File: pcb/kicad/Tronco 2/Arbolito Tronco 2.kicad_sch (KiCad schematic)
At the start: 18 parts, among them U1 WS2812B, U10 WS2812B, U11 WS2812B, U12 WS2812B, U2 WS2812B, U3 WS2812B, U4 WS2812B, U5 WS2812B, U6 WS2812B, U7 WS2812B, U8 WS2812B, U9 WS2812B

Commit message: Do some cleaning and add .gitignore
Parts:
- removed C3, C4: 0.1uF, Capacitor_SMD:C_0805_2012Metric, symbol Device:C
- removed U1, U11, U12, U2, U5, U6, U7, U8: WS2812B, LED_SMD:LED_WS2812B_PLCC4_5.0x5.0mm_P3.2mm, symbol WB2182:WS2812B
- added J1, J2, J3, J4, J5, J6: Conn_01x01, Library:Output, symbol Connector_Generic:Conn_01x01
- U1: renamed from U3; footprint LED_SMD:LED_WS2812B_PLCC4_5.0x5.0mm_P3.2mm -> Library:LED_WS2812B_PLCC4_5.0x5.0mm_P3.2mm
- U2: renamed from U4; footprint LED_SMD:LED_WS2812B_PLCC4_5.0x5.0mm_P3.2mm -> Library:LED_WS2812B_PLCC4_5.0x5.0mm_P3.2mm
- U3: renamed from U9; footprint LED_SMD:LED_WS2812B_PLCC4_5.0x5.0mm_P3.2mm -> Library:LED_WS2812B_PLCC4_5.0x5.0mm_P3.2mm
- U4: renamed from U10; footprint LED_SMD:LED_WS2812B_PLCC4_5.0x5.0mm_P3.2mm -> Library:LED_WS2812B_PLCC4_5.0x5.0mm_P3.2mm
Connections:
- net +5V: now also J3.1 (Pin_1), J4.1 (Pin_1)
- net DIN: now also U1.4 (DIN), J1.1 (Pin_1), J2.1 (Pin_1)
- net GND: now also J5.1 (Pin_1), J6.1 (Pin_1)
- net at U2.2 (DOUT): now also U3.4 (DIN)

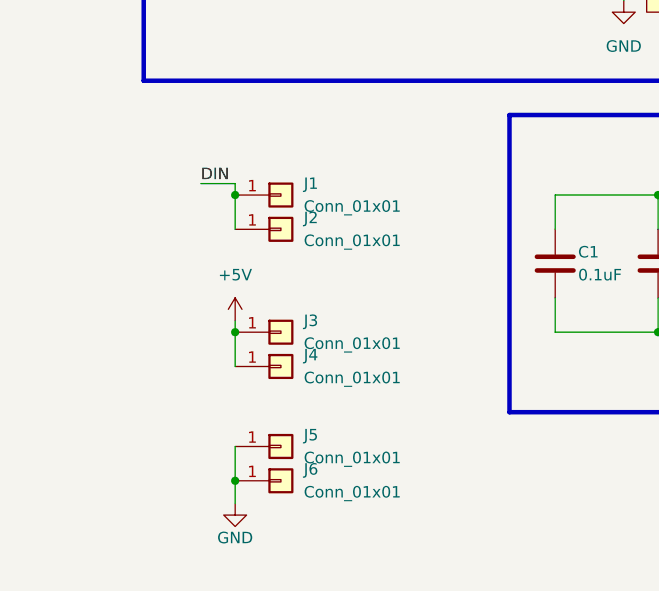
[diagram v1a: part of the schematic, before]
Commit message: DRC Errors fixeds
The WS218B double footprint was remade in order to avoid DRC errors :3
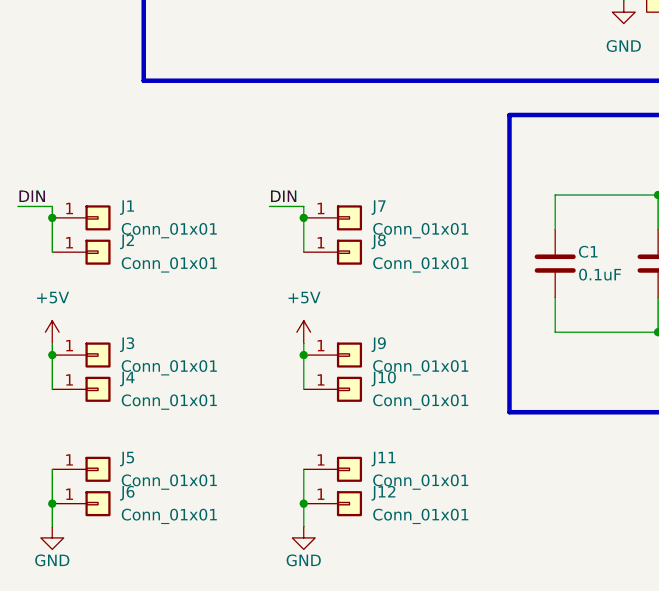
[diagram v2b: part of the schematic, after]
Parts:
- added J10, J11, J12, J7, J8, J9: Conn_01x01, Library:Output, symbol Connector_Generic:Conn_01x01
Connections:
- net +5V: now also J10.1 (Pin_1), J9.1 (Pin_1)
- net DIN: now also J7.1 (Pin_1), J8.1 (Pin_1)
- net GND: now also J11.1 (Pin_1), J12.1 (Pin_1)
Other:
- moved on the sheet: J1, J2, J3, J4, J5, J6
